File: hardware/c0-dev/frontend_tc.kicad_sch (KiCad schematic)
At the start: 72 parts, among them U501 B0505S-1WR3, U502 ISO1540, U503 ISO1540, U504 TMP117xxDRV, U505 AMS1117-3.3, U506 TMP117xxDRV, U507 ADS1015IDGS, U508 ADS1015IDGS

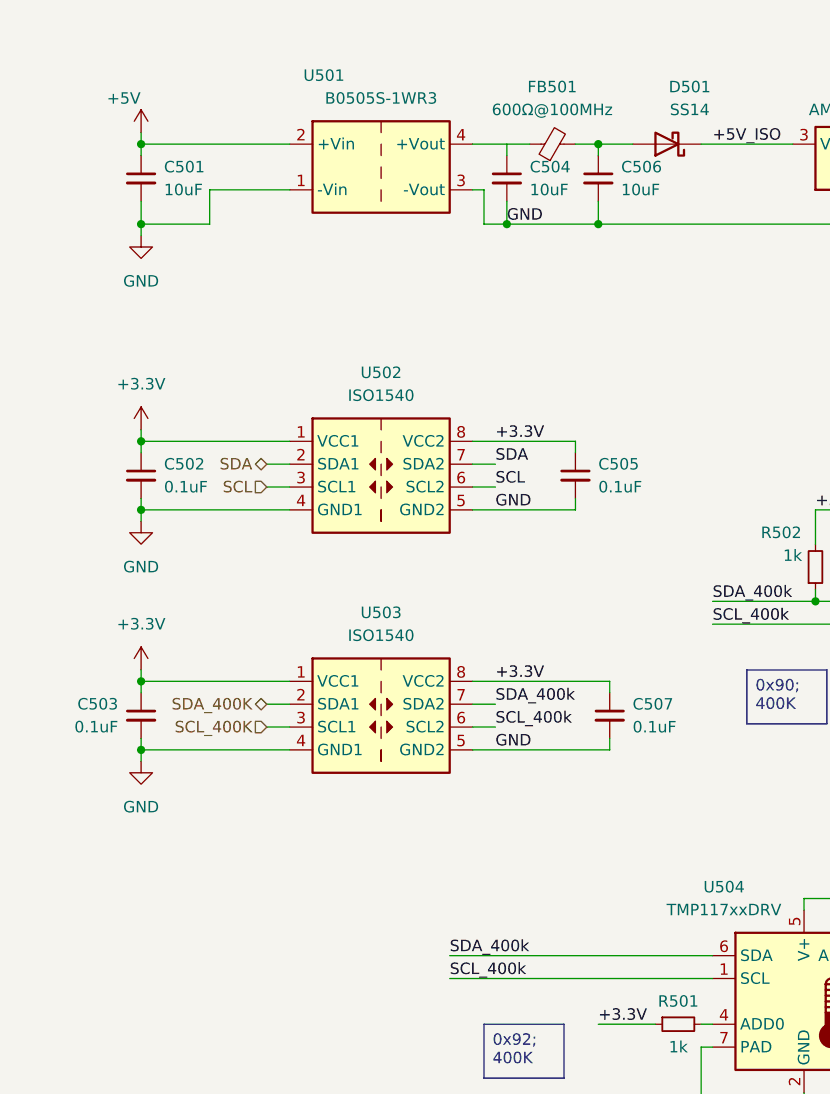
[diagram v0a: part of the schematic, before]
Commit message: silkscreen, isolation and placement cleanup
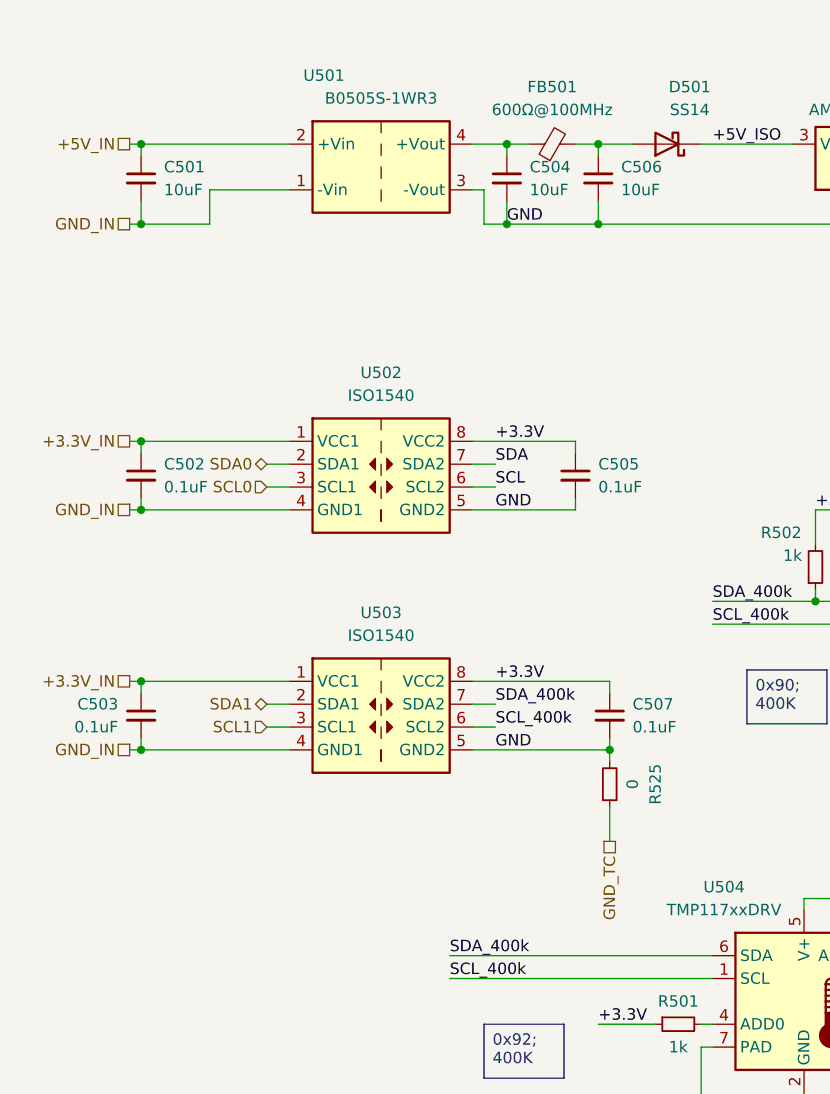
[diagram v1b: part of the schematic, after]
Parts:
- added R525: 0, Resistor_SMD:R_0402_1005Metric, symbol Device:R_Small
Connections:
- net +3.3V: no longer C502.1, C503.1, U502.1 (VCC1), U503.1 (VCC1)
- net GND: now also R525.2; no longer C501.2, C502.2, C503.2, U501.1 (-Vin), U502.4 (GND1), U503.4 (GND1)
- net SCL: no longer U502.3 (SCL1)
- net SDA: no longer U502.2 (SDA1)
- net at FB501.1, U501.4 (+Vout): now also C504.1
- net +5V renamed +5V_IN
- net SCL_400K renamed SCL1
- net SDA_400K renamed SDA1
- new net +3.3V_IN: C502.1, C503.1, U502.1 (VCC1), U503.1 (VCC1)
- new net GND_IN: C501.2, C502.2, C503.2, U501.1 (-Vin), U502.4 (GND1), U503.4 (GND1)
- new net GND_TC: R525.1
- new net SCL0: U502.3 (SCL1)
- new net SDA0: U502.2 (SDA1)

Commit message: added 3d models
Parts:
- U501: footprint Converter_DCDC:Converter_DCDC_Murata_MEE1SxxxxSC_THT -> conduit:Converter_DCDC_EVISUN_BXXXXS-1WR3
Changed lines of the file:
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@@
 			)
 		)
-		(property "Footprint" "Converter_DCDC:Converter_DCDC_Murata_MEE1SxxxxSC_THT"
+		(property "Footprint" "conduit:Converter_DCDC_EVISUN_BXXXXS-1WR3"
 			(at 25.4 36.83 0)
 			(hide yes)
